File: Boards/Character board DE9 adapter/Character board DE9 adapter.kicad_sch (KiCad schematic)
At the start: 2 parts, among them J1 DE9_Plug_MountingHoles, J2 character connector

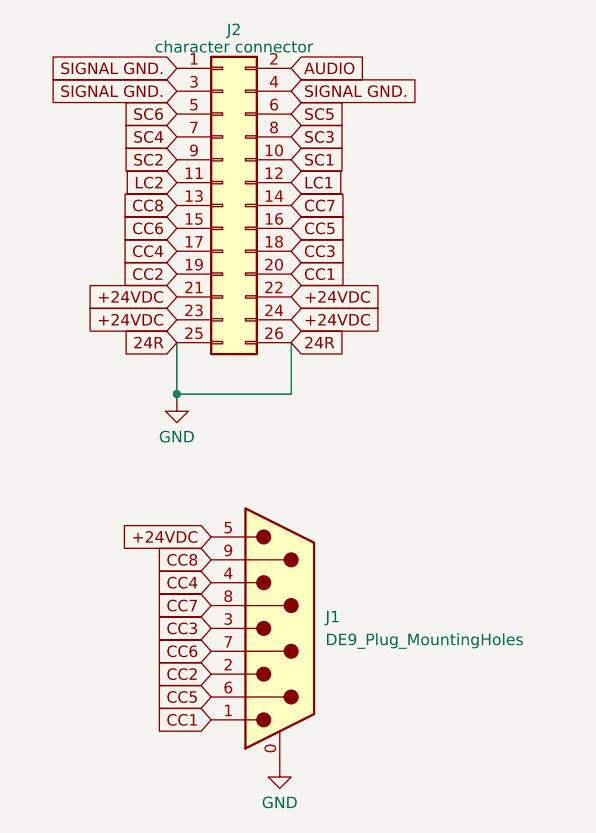
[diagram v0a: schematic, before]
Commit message: added audio board schematics and de9 board fab files
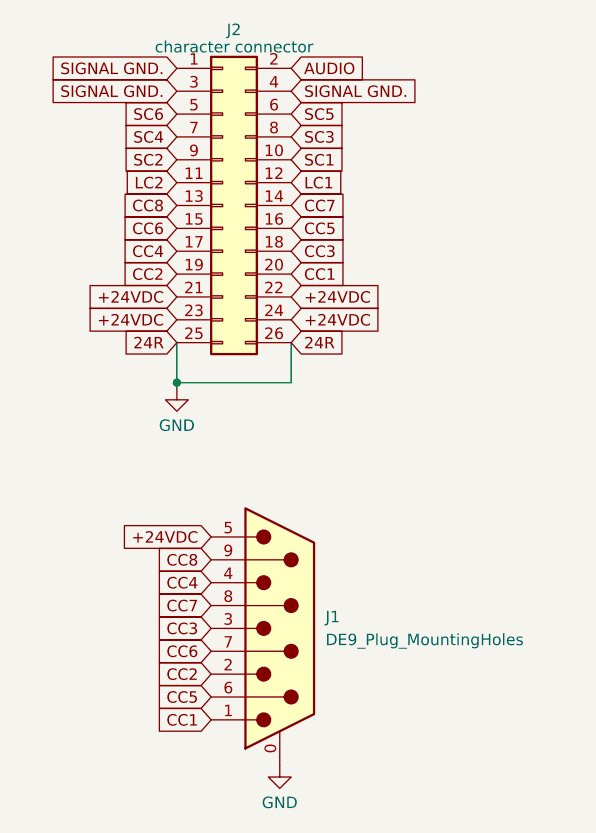
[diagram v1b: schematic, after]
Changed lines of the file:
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@@
 	(paper "A4")
 	(junction
-		(at 118.11 93.345)
+		(at 118.11 92.075)
 		(diameter 0)
 		(color 0 0 0 0)
@@
 	(wire
 		(pts
-			(xy 130.81 93.345) (xy 118.11 93.345)
+			(xy 130.81 92.075) (xy 118.11 92.075)
 		)
 		(stroke
@@
 	(wire
 		(pts
-			(xy 130.81 93.345) (xy 130.81 87.63)
+			(xy 130.81 92.075) (xy 130.81 87.63)
 		)
 		(stroke
@@
 	(wire
 		(pts
-			(xy 118.11 93.98) (xy 118.11 93.345)
+			(xy 118.11 92.71) (xy 118.11 92.075)
 		)
 		(stroke
@@
 	(wire
 		(pts
-			(xy 118.11 93.345) (xy 118.11 87.63)
+			(xy 118.11 92.075) (xy 118.11 87.63)
 		)
 		(stroke
@@
 	(symbol
 		(lib_id "power:GND")
-		(at 118.11 93.98 0)
+		(at 118.11 92.71 0)
 		(unit 1)
 		(exclude_from_sim no)
@@
 		(fields_autoplaced yes)
 		(property "Reference" "#PWR02"
-			(at 118.11 100.33 0)
+			(at 118.11 99.06 0)
 			(effects
 				(font
@@
 		)
 		(property "Value" "GND"
-			(at 118.11 98.1155 0)
+			(at 118.11 96.8455 0)
 			(effects
 				(font
@@
 		)
 		(property "Footprint" ""
-			(at 118.11 93.98 0)
+			(at 118.11 92.71 0)
 			(effects
 				(font
@@
 		)
 		(property "Datasheet" ""
-			(at 118.11 93.98 0)
+			(at 118.11 92.71 0)
 			(effects
 				(font
@@
 		)
 		(property "Description" ""
-			(at 118.11 93.98 0)
-			(effects
-				(font
+			(at 118.11 92.71 0)
+			(effects
+				(font
